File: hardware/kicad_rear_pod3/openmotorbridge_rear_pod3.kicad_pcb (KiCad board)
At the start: 4 copper layers, 50 x 35 mm, 25 parts, among them J1 M8_3PIN_SOCKET, U1 ESP32-C3-WROOM-02, U2 MAX-M10S, U3 SX1262

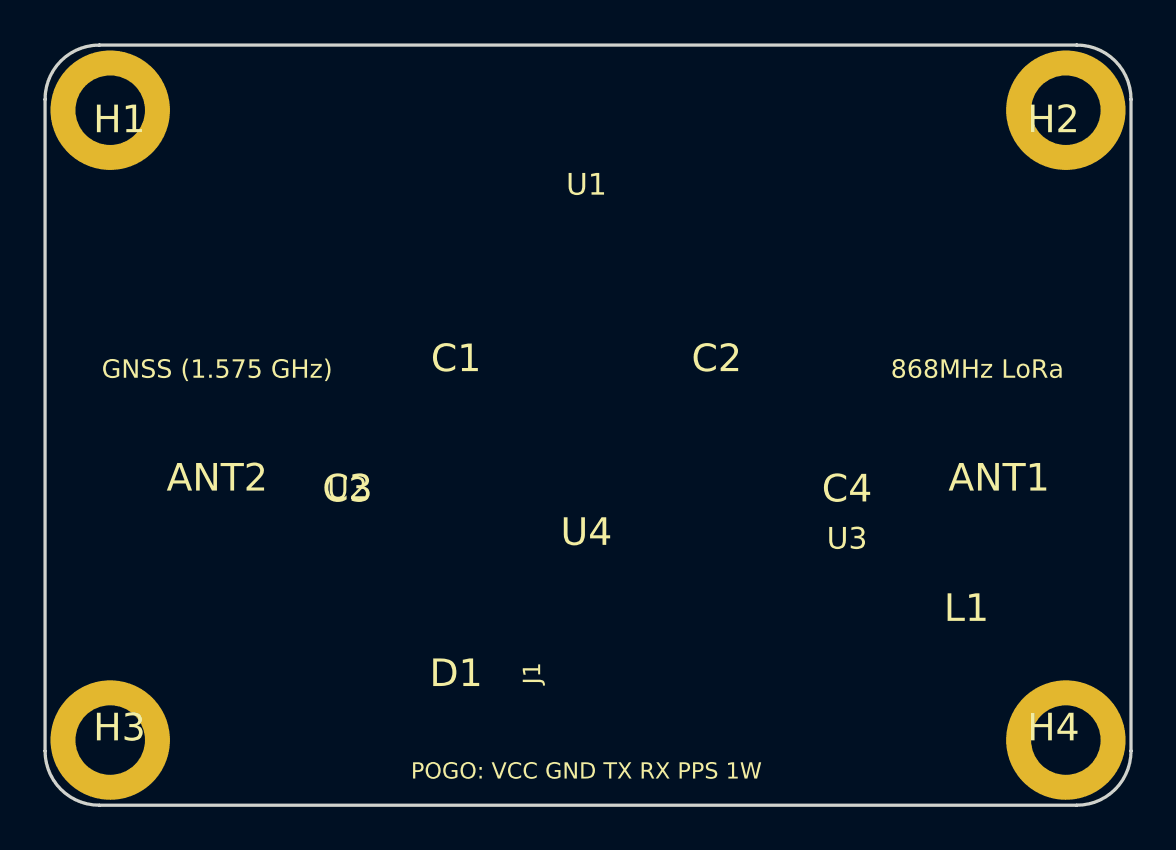
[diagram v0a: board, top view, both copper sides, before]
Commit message: fix(hardware): finalize Rear Pod 3 layout with wide component clearances, flush antenna and horizontal 6-pin Pogo interface
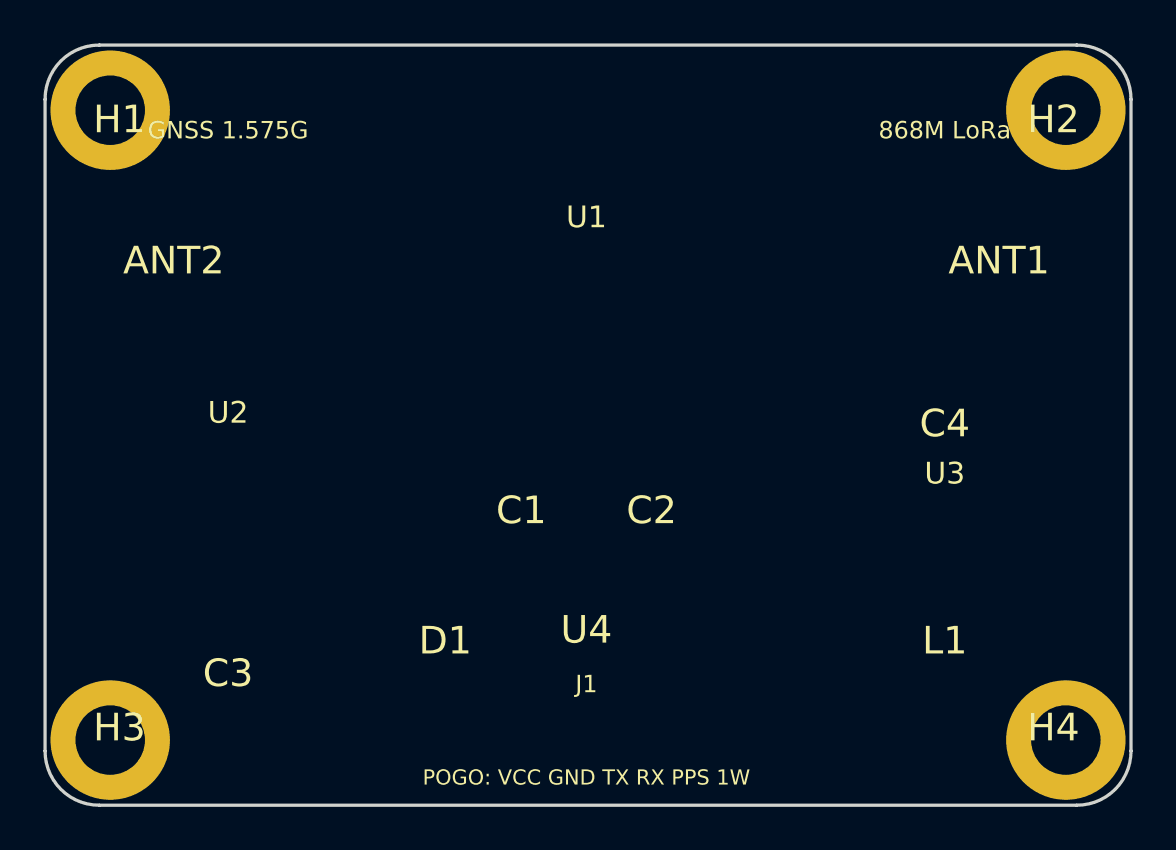
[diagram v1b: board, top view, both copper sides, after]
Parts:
- moved ANT2 10.2 mm to (106.0, 80.0)
- moved C3 10.1 mm to (108.5, 99.0)
- moved ANT1 10.0 mm to (144.0, 80.0)
- moved C1 7.62 mm to (122.0, 91.5)
- moved C2 7.62 mm to (128.0, 91.5)
- moved U2 6.52 mm to (108.5, 93.0)
- moved C4 5.41 mm to (141.5, 87.5)
- moved U3 5.41 mm to (141.5, 93.0)
- moved U4 4.50 mm to (125.0, 97.0)
- moved J1 3.00 mm to (125.0, 102.0), turned to 0 degrees
- moved L1 1.80 mm to (141.5, 97.5)
- moved D1 1.58 mm to (118.5, 97.5)
- moved U1 1.50 mm to (125.0, 86.0)
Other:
- board text added: "868M LoRa"
- board text added: "GNSS 1.575G"
- board text removed: "868MHz LoRa"
- board text removed: "GNSS (1.575 GHz)"
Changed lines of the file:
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@@
 	(footprint "RF_Module:ESP32-C3-WROOM-02"
 		(layer "F.Cu")
-		(at 125 84.5)
+		(at 125 86)
 		(property "Reference" "U1"
 			(at 0 -8 0)
@@
 	(footprint ""
 		(layer "F.Cu")
-		(at 142.5 96)
+		(at 141.5 97.5)
 		(property "Reference" "L1"
 			(at 0 0 0)
@@
 	(footprint ""
 		(layer "F.Cu")
-		(at 144 90)
+		(at 144 80)
 		(property "Reference" "ANT1"
 			(at 0 0 0)
@@
 	(footprint ""
 		(layer "F.Cu")
-		(at 114 90.5)
+		(at 108.5 99)
 		(property "Reference" "C3"
 			(at 0 0 0)
@@
 	(footprint "RF_GPS:u-blox_MAX-M10S"
 		(layer "F.Cu")
-		(at 114 96.5)
+		(at 108.5 93)
 		(property "Reference" "U2"
 			(at 0 -6 0)
@@
 	(footprint ""
 		(layer "F.Cu")
-		(at 131 84.5)
+		(at 128 91.5)
 		(property "Reference" "C2"
 			(at 0 0 0)
@@
 	(footprint ""
 		(layer "F.Cu")
-		(at 125 92.5)
+		(at 125 97)
 		(property "Reference" "U4"
 			(at 0 0 0)
@@
 	(footprint ""
 		(layer "F.Cu")
-		(at 108 90)
+		(at 106 80)
 		(property "Reference" "ANT2"
 			(at 0 0 0)
@@
 	(footprint ""
 		(layer "F.Cu")
-		(at 119 99)
+		(at 118.5 97.5)
 		(property "Reference" "D1"
 			(at 0 0 0)
@@
 	(footprint ""
 		(layer "F.Cu")
-		(at 119 84.5)
+		(at 122 91.5)
 		(property "Reference" "C1"
 			(at 0 0 0)
@@
 	(footprint "Package_DFN_QFN:QFN-24-1EP_4x4mm_P0.5mm_EP2.6x2.6mm"
 		(layer "F.Cu")
-		(at 137 96)
+		(at 141.5 93)
 		(property "Reference" "U3"
 			(at 0 -3.2 0)
@@
 	(footprint "Connector_PinHeader_2.54mm:PinHeader_1x03_P2.54mm_Vertical"
 		(layer "F.Cu")
-		(at 125 99 90)
+		(at 125 102)
 		(property "Reference" "J1"
-			(at 0 -2.5 90)
+			(at 0 -2.5 0)
 			(layer "F.SilkS")
 			(effects
@@
 		)
 		(property "Value" "M8_3PIN_SOCKET"
-			(at 0 2.5 90)
+			(at 0 2.5 0)
 			(layer "F.Fab")
 			(effects
@@
 		)
 		(property "Datasheet" ""
-			(at 0 0 90)
-			(layer "F.Fab")
-			(hide yes)
-			(effects
-				(font
-					(size 1.27 1.27)
-				)
-			)
-		)
-		(property "Description" ""
-			(at 0 0 90)
+			(at 0 0 0)
+			(layer "F.Fab")
+			(hide yes)
+			(effects
+				(font
+					(size 1.27 1.27)
+				)
+			)
+		)
+		(property "Description" ""
+			(at 0 0 0)
 			(layer "F.Fab")
 			(hide yes)
@@
 	(footprint ""
 		(layer "F.Cu")
-		(at 137 90.5)
+		(at 141.5 87.5)
 		(property "Reference" "C4"
 			(at 0 0 0)
@@
 	)
 	(gr_text "POGO: VCC GND TX RX PPS 1W"
-		(at 125 103.5 0)
+		(at 125 103.8 0)
 		(layer "F.SilkS")
 		(effects
 			(font
-				(size 0.75 0.75)
-				(thickness 0.14)
-			)
-		)
-	)
-	(gr_text "GNSS (1.575 GHz)"
-		(at 108 85 0)
+				(size 0.7 0.7)
+				(thickness 0.13)
+			)
+		)
+	)
+	(gr_text "GNSS 1.575G"
+		(at 108.5 74 0)
 		(layer "F.SilkS")
 		(effects
 			(font
-				(size 0.85 0.85)
+				(size 0.8 0.8)
 				(thickness 0.15)
 			)
 		)
 	)
-	(gr_text "868MHz LoRa"
-		(at 143 85 0)
+	(gr_text "868M LoRa"
+		(at 141.5 74 0)
 		(layer "F.SilkS")
 		(effects
 			(font
-				(size 0.85 0.85)
+				(size 0.8 0.8)
 				(thickness 0.15)
 			)

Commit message: feat(hardware): update Rear Pod 3 OMM transceiver PCB with bottom mating socket, symmetrical top RF layout, and updated 3D renders
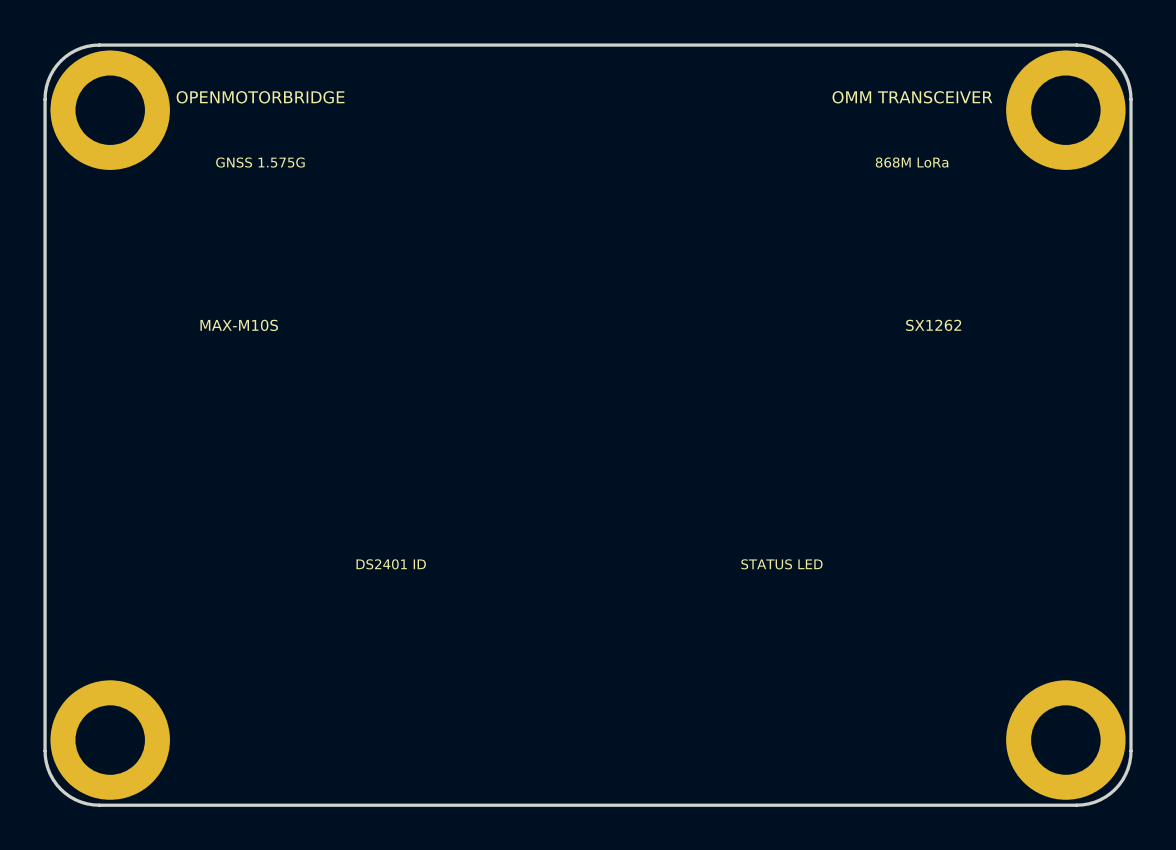
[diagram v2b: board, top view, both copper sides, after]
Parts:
- J1: moved to B.Cu
- moved D1 15.5 mm to (134.0, 98.0)
- moved U4 9.06 mm to (116.0, 98.0)
- moved C4 9.01 mm to (141.0, 96.5)
- moved U1 8.00 mm to (125.0, 78.0)
- moved C3 5.02 mm to (109.0, 94.0)
- moved U2 5.02 mm to (109.0, 88.0)
- moved U3 5.02 mm to (141.0, 88.0)
- moved L1 4.03 mm to (141.0, 93.5)
- moved J1 4.00 mm to (125.0, 98.0)
- moved ANT1 2.83 mm to (142.0, 78.0)
- moved ANT2 2.83 mm to (108.0, 78.0)
- moved C1 2.69 mm to (121.0, 89.0)
- moved C2 2.69 mm to (129.0, 89.0)
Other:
- board text added: "6-PIN SOCKET (MATES TO POD-BASE)"
- board text added: "DS2401 ID"
- board text added: "FACTORY TESTPOINTS (PROD FLASH)"
- board text added: "MAX-M10S"
- board text added: "OMM TRANSCEIVER"
- board text added: "OPENMOTORBRIDGE"
- board text added: "STATUS LED"
- board text added: "SX1262"
- board text removed: "POGO: VCC GND TX RX PPS 1W"

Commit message: fix(hardware): eliminate ESP32 antenna overhang and route all passives to wings on Rear Pod 3 OMM PCB
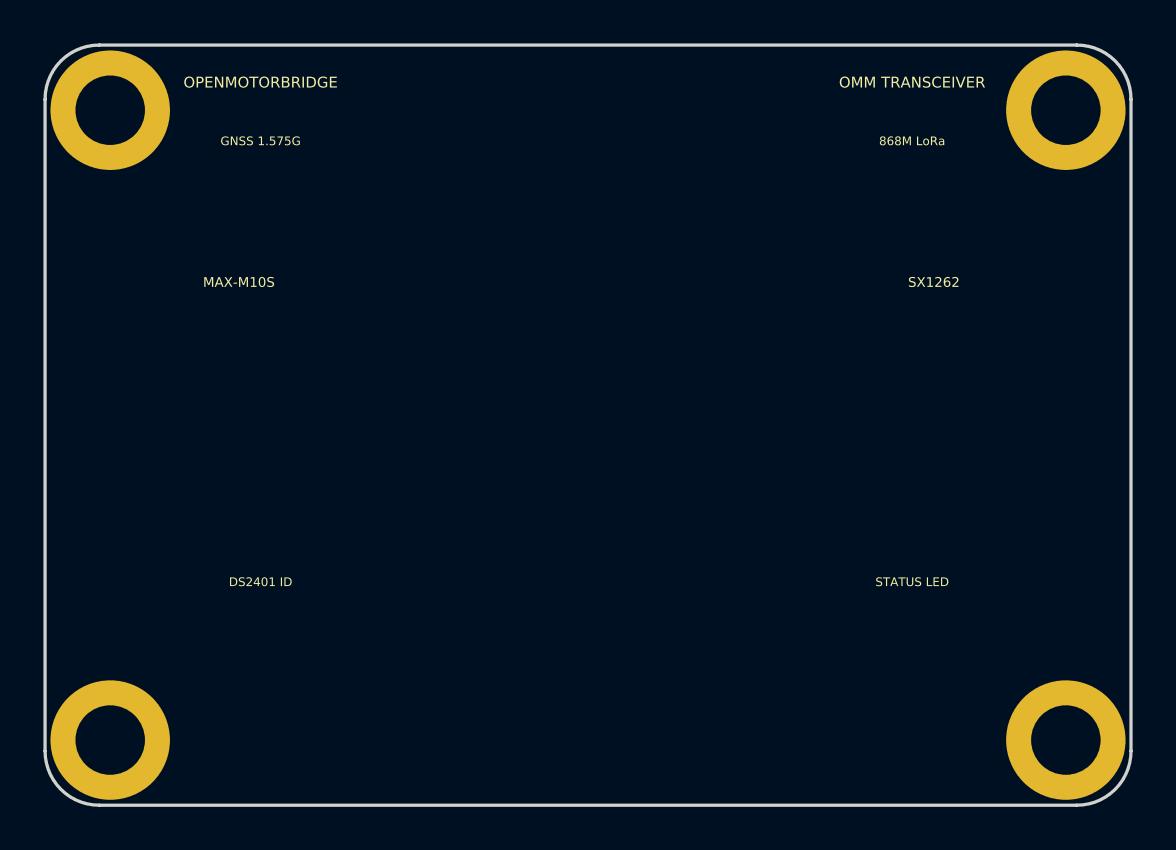
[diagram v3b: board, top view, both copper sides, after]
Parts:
- moved C1 8.28 mm to (113.5, 92.5)
- moved C2 8.28 mm to (136.5, 92.5)
- moved U1 8.00 mm to (125.0, 86.0)
- moved C4 6.73 mm to (145.5, 91.5)
- moved D1 6.00 mm to (140.0, 98.0)
- moved U4 6.00 mm to (110.0, 98.0)
- moved C3 2.50 mm to (109.0, 91.5)
- moved J1 2.50 mm to (125.0, 100.5), turned to 90 degrees
- moved ANT1 2.00 mm to (142.0, 76.0)
- moved ANT2 2.00 mm to (108.0, 76.0)
- moved L1 2.00 mm to (141.0, 91.5)
- moved TP1 2.00 mm to (115.0, 78.0)
- moved TP2 2.00 mm to (118.0, 78.0)
- moved TP3 2.00 mm to (132.0, 78.0)
- moved TP4 2.00 mm to (135.0, 78.0)
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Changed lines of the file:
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@@
 	(footprint "RF_Module:ESP32-C3-WROOM-02"
 		(layer "F.Cu")
-		(at 125 78)
+		(at 125 86)
 		(property "Reference" "U1"
 			(at 0 -8 0)
@@
 	(footprint ""
 		(layer "F.Cu")
-		(at 141 93.5)
+		(at 141 91.5)
 		(property "Reference" "L1"
 			(at 0 0 0)
@@
 	(footprint ""
 		(layer "F.Cu")
-		(at 142 78)
+		(at 142 76)
 		(property "Reference" "ANT1"
 			(at 0 0 0)
@@
 	(footprint ""
 		(layer "F.Cu")
-		(at 109 94)
+		(at 109 91.5)
 		(property "Reference" "C3"
 			(at 0 0 0)
@@
 	(footprint "RF_GPS:u-blox_MAX-M10S"
 		(layer "F.Cu")
-		(at 109 88)
+		(at 109 86)
 		(property "Reference" "U2"
 			(at 0 -6 0)
@@
 	(footprint ""
 		(layer "F.Cu")
-		(at 129 89)
+		(at 136.5 92.5)
 		(property "Reference" "C2"
 			(at 0 0 0)
@@
 	(footprint ""
 		(layer "F.Cu")
-		(at 116 98)
+		(at 110 98)
 		(property "Reference" "U4"
 			(at 0 0 0)
@@
 	(footprint ""
 		(layer "F.Cu")
-		(at 108 78)
+		(at 108 76)
 		(property "Reference" "ANT2"
 			(at 0 0 0)
@@
 	(footprint ""
 		(layer "F.Cu")
-		(at 134 98)
+		(at 140 98)
 		(property "Reference" "D1"
 			(at 0 0 0)
@@
 	(footprint ""
 		(layer "F.Cu")
-		(at 121 89)
+		(at 113.5 92.5)
 		(property "Reference" "C1"
 			(at 0 0 0)
@@
 	(footprint "Package_DFN_QFN:QFN-24-1EP_4x4mm_P0.5mm_EP2.6x2.6mm"
 		(layer "F.Cu")
-		(at 141 88)
+		(at 141 86)
 		(property "Reference" "U3"
 			(at 0 -3.2 0)
@@
 	(footprint ""
 		(layer "F.Cu")
-		(at 141 96.5)
+		(at 145.5 91.5)
 		(property "Reference" "C4"
 			(at 0 0 0)
@@
 	(footprint ""
 		(layer "B.Cu")
-		(at 135 80)
+		(at 135 78)
 		(property "Reference" "TP4"
 			(at 0 0 0)
@@
 	(footprint ""
 		(layer "B.Cu")
-		(at 132 80)
+		(at 132 78)
 		(property "Reference" "TP3"
 			(at 0 0 0)
@@
 	(footprint ""
 		(layer "B.Cu")
-		(at 118 80)
+		(at 118 78)
 		(property "Reference" "TP2"
 			(at 0 0 0)
@@
 	(footprint "Connector_PinHeader_2.54mm:PinHeader_1x03_P2.54mm_Vertical"
 		(layer "B.Cu")
-		(at 125 98)
+		(at 125 100.5 90)
 		(property "Reference" "J1"
-			(at 0 -2.5 0)
+			(at 0 -2.5 90)
 			(layer "F.SilkS")
 			(hide yes)
@@
 		)
 		(property "Value" "M8_3PIN_SOCKET"
-			(at 0 2.5 0)
+			(at 0 2.5 90)
 			(layer "F.Fab")
 			(effects
@@
 		)
 		(property "Datasheet" ""
-			(at 0 0 0)
-			(layer "F.Fab")
-			(hide yes)
-			(effects
-				(font
-					(size 1.27 1.27)
-				)
-			)
-		)
-		(property "Description" ""
-			(at 0 0 0)
+			(at 0 0 90)
+			(layer "F.Fab")
+			(hide yes)
+			(effects
+				(font
+					(size 1.27 1.27)
+				)
+			)
+		)
+		(property "Description" ""
+			(at 0 0 90)
 			(layer "F.Fab")
 			(hide yes)
@@
 	(footprint ""
 		(layer "B.Cu")
-		(at 115 80)
+		(at 115 78)
 		(property "Reference" "TP1"
 			(at 0 0 0)
@@
 	)
 	(gr_text "GNSS 1.575G"
-		(at 110 75.5 0)
+		(at 110 74.5 0)
+		(layer "F.SilkS")
+		(effects
+			(font
+				(size 0.4 0.4)
+				(thickness 0.09)
+			)
+		)
+	)
+	(gr_text "DS2401 ID"
+		(at 110 94.8 0)
+		(layer "F.SilkS")
+		(effects
+			(font
+				(size 0.4 0.4)
+				(thickness 0.09)
+			)
+		)
+	)
+	(gr_text "868M LoRa"
+		(at 140 74.5 0)
+		(layer "F.SilkS")
+		(effects
+			(font
+				(size 0.4 0.4)
+				(thickness 0.09)
+			)
+		)
+	)
+	(gr_text "STATUS LED"
+		(at 140 94.8 0)
+		(layer "F.SilkS")
+		(effects
+			(font
+				(size 0.4 0.4)
+				(thickness 0.09)
+			)
+		)
+	)
+	(gr_text "MAX-M10S"
+		(at 109 81 0)
 		(layer "F.SilkS")
 		(effects
@@
 		)
 	)
-	(gr_text "DS2401 ID"
-		(at 116 94 0)
+	(gr_text "SX1262"
+		(at 141 81 0)
 		(layer "F.SilkS")
 		(effects
@@
 		)
 	)
-	(gr_text "STATUS LED"
-		(at 134 94 0)
-		(layer "F.SilkS")
-		(effects
-			(font
-				(size 0.45 0.45)
-				(thickness 0.1)
-			)
-		)
-	)
-	(gr_text "868M LoRa"
-		(at 140 75.5 0)
-		(layer "F.SilkS")
-		(effects
-			(font
-				(size 0.45 0.45)
-				(thickness 0.1)
-			)
-		)
-	)
-	(gr_text "MAX-M10S"
-		(at 109 83 0)
+	(gr_text "OPENMOTORBRIDGE"
+		(at 110 71.8 0)
 		(layer "F.SilkS")
 		(effects
 			(font
 				(size 0.5 0.5)
-				(thickness 0.1)
-			)
-		)
-	)
-	(gr_text "SX1262"
-		(at 141 83 0)
+				(thickness 0.11)
+			)
+		)
+	)
+	(gr_text "OMM TRANSCEIVER"
+		(at 140 71.8 0)
 		(layer "F.SilkS")
 		(effects
 			(font
 				(size 0.5 0.5)
-				(thickness 0.1)
-			)
-		)
-	)
-	(gr_text "OPENMOTORBRIDGE"
-		(at 110 72.5 0)
-		(layer "F.SilkS")
-		(effects
-			(font
-				(size 0.55 0.55)
-				(thickness 0.12)
-			)
-		)
-	)
-	(gr_text "OMM TRANSCEIVER"
-		(at 140 72.5 0)
-		(layer "F.SilkS")
-		(effects
-			(font
-				(size 0.55 0.55)
-				(thickness 0.12)
+				(thickness 0.11)
 			)
 		)
 	)
 	(gr_text "FACTORY TESTPOINTS (PROD FLASH)"
-		(at 125 75 0)
+		(at 125 74 0)
 		(layer "B.SilkS")
 		(effects
 			(font
-				(size 0.5 0.5)
+				(size 0.45 0.45)
 				(thickness 0.1)
 			)
@@
 		(effects
 			(font
-				(size 0.55 0.55)
-				(thickness 0.12)
-			)
-		)
+				(size 0.5 0.5)
+				(thickness 0.11)
+			)
+		)
